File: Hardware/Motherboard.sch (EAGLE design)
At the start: 66 parts, among them J1 MICROMOD-2222-C, J10 MICRO-SD-PUSH-PUSH-EXT-PIN, J2 Vertical Qwiic Connector, J4 QWIIC_RIGHT_ANGLE, J5 CORTEX_JTAG_DEBUG_MINIMUM_PTH, J6 MICROMOD_CARRIER, J7 MICROMOD_CARRIER, U2 MCP73831, U5 AP7361C-33

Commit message: Adds second standoff for qwiic boards, attaches VIN net to processor connector
Deletes second page in schematic
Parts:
- removed FRAME2: FRAME-LEDGERNO_FOOTPRINT, SparkFun-Aesthetics:FRAME-LEDGERNO_FOOTPRINT
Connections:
- removed net USB_VIN: J1.USB_VIN
- net VIN: now also J1.USB_VIN
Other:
- note added: "Buttons"

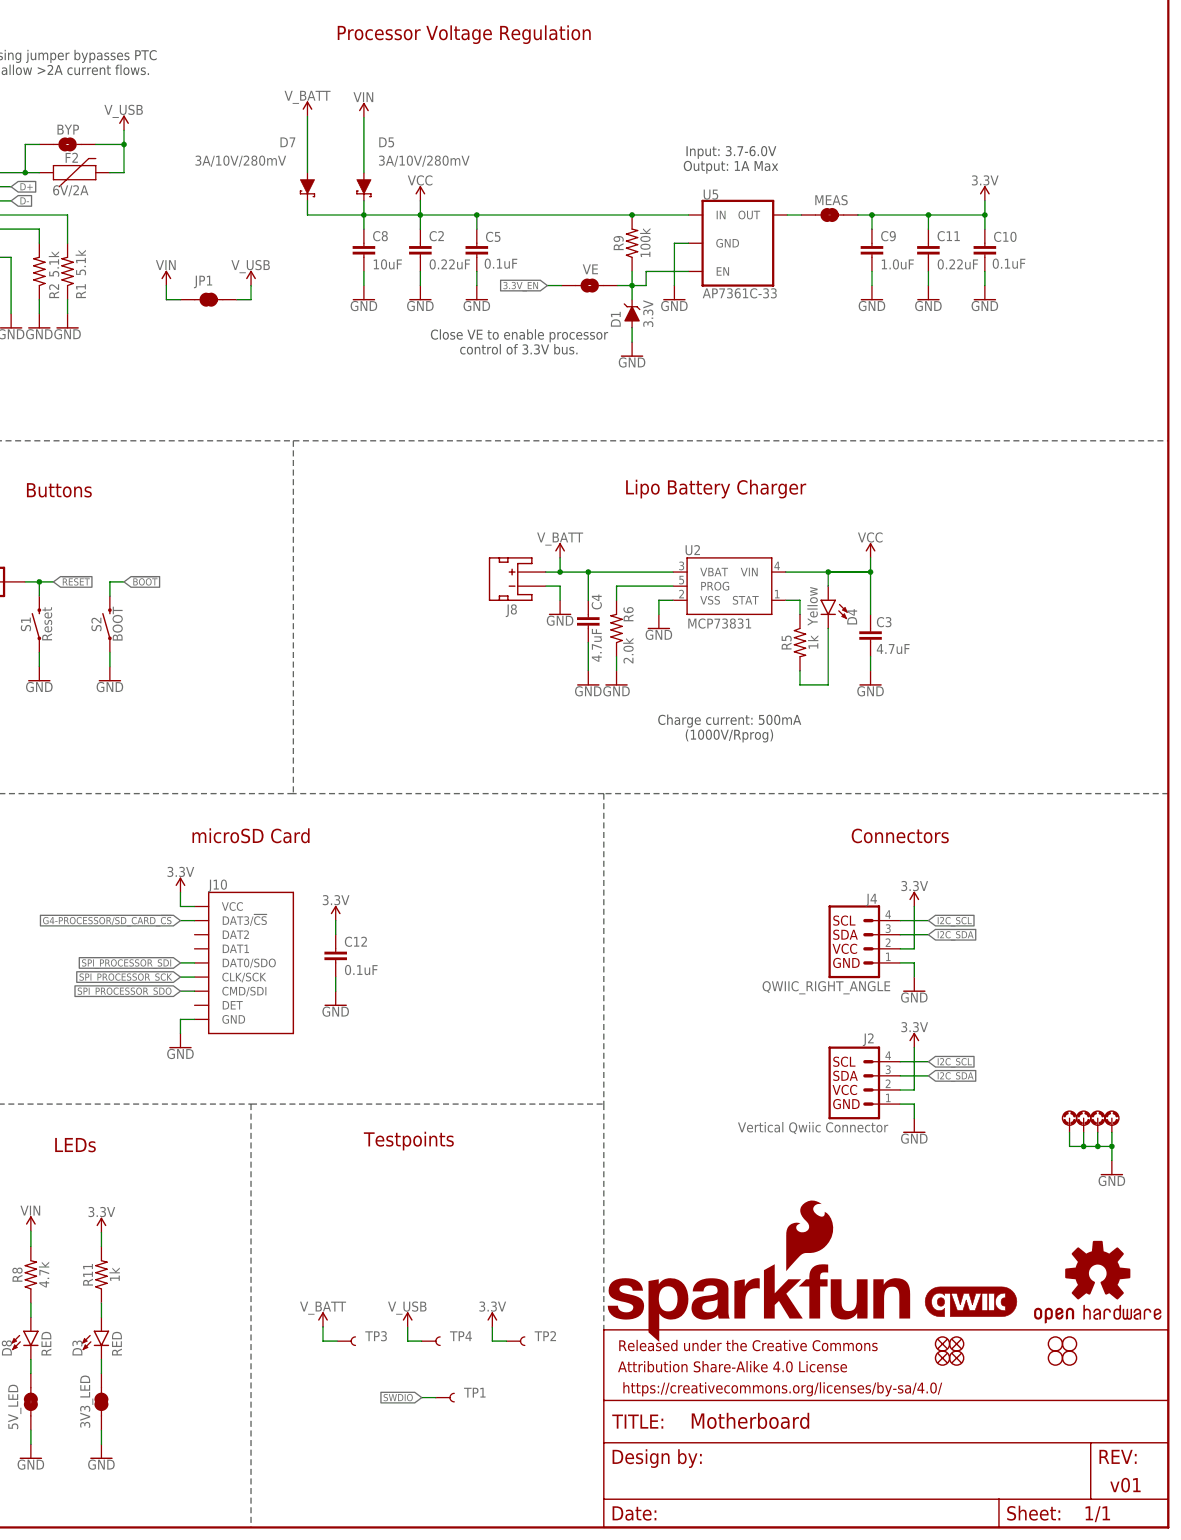
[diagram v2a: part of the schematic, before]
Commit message: Adds silk, removes "VIN/VUSB" jumper
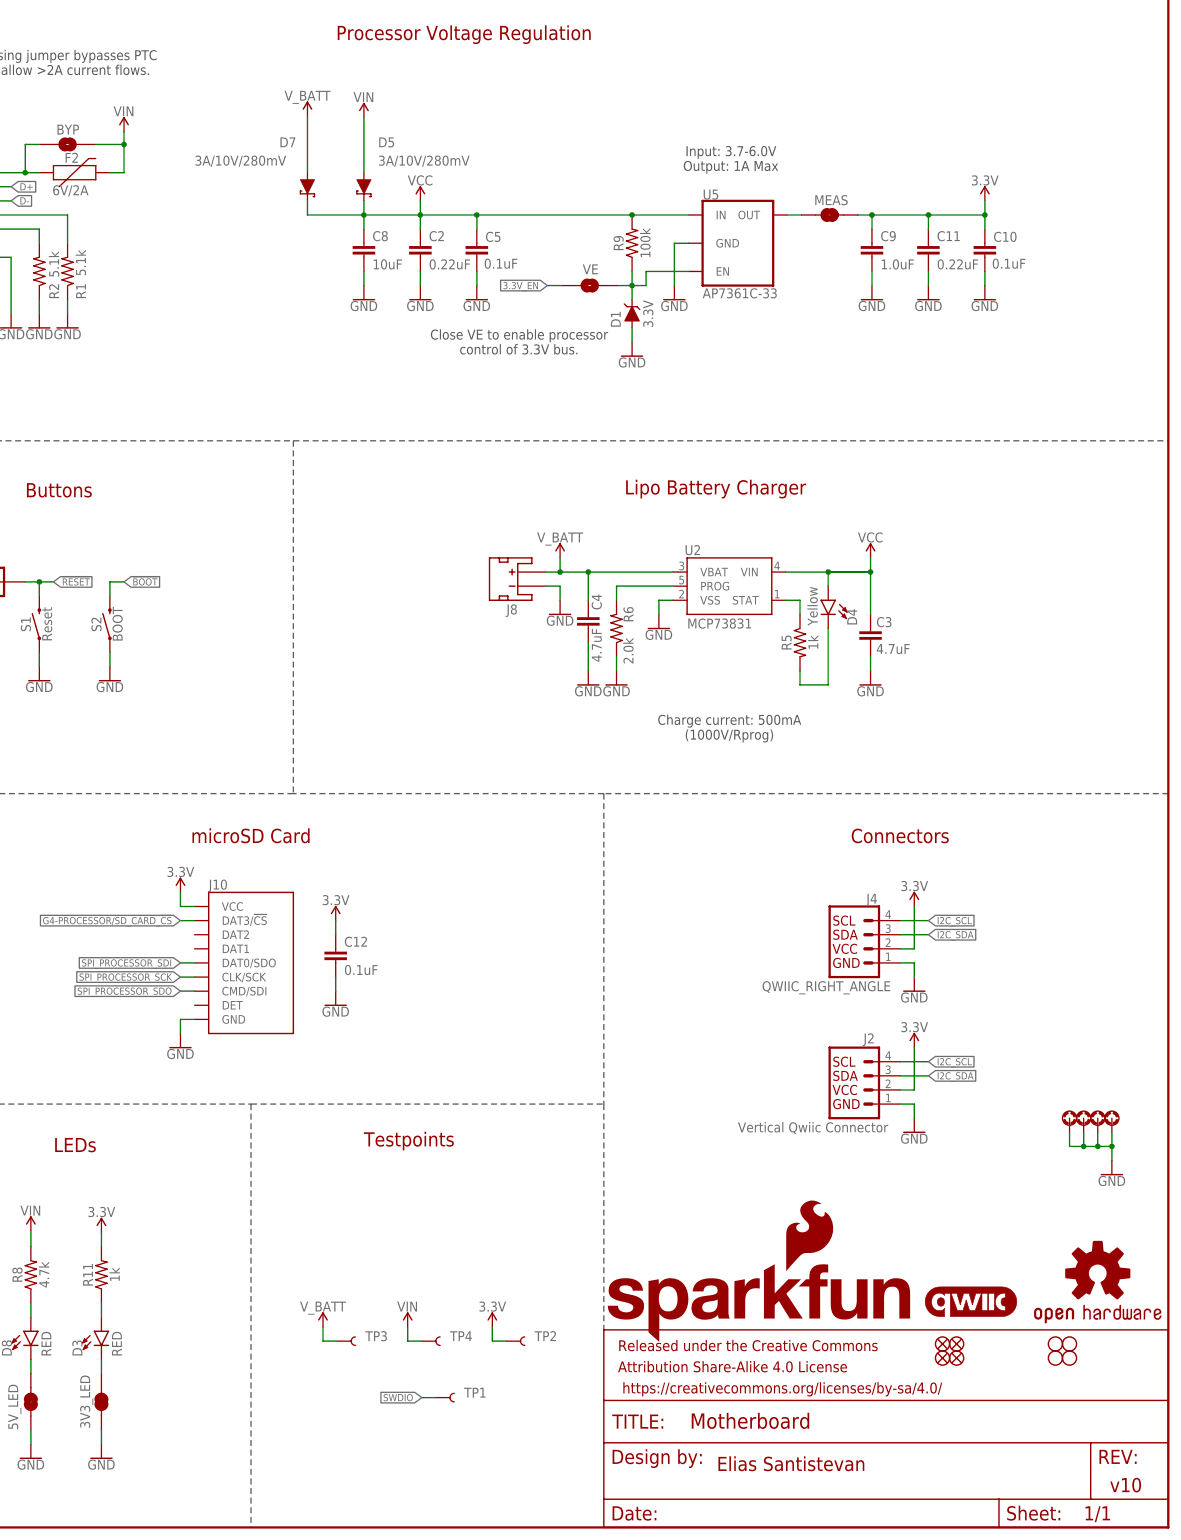
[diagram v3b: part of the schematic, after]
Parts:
- removed JP1: JUMPER-SMT_2_NC_TRACE_SILK, SparkFun-Jumpers:JUMPER-SMT_2_NC_TRACE_SILK
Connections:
- removed net V_USB: BYP.2, F2.2, JP1.2, TP4.1
- net VIN: now also BYP.2, F2.2, TP4.1; no longer JP1.1
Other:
- note added: "Elias Santistevan"
- note added: "v10"
- note removed: "v01"
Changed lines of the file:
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@@
 <?xml version="1.0" encoding="utf-8"?>
 <!DOCTYPE eagle SYSTEM "eagle.dtd">
-<eagle version="9.5.1">
+<eagle version="9.6.2">
 <drawing>
 <settings>
@@
 <part name="SUPPLY23" library="SparkFun-PowerSymbols" deviceset="VIN" device=""/>
 <part name="SUPPLY4" library="SparkFun-PowerSymbols" deviceset="VIN" device=""/>
-<part name="JP1" library="SparkFun-Jumpers" deviceset="JUMPER-SMT_2_NC_TRACE" device="_SILK" package3d_urn="urn:adsk.eagle:package:39281/1"/>
-<part name="SUPPLY18" library="SparkFun-PowerSymbols" deviceset="VIN" device=""/>
-<part name="SUPPLY21" library="SparkFun-PowerSymbols" deviceset="V_USB" device=""/>
 <part name="LOGO2" library="SparkFun-Aesthetics" deviceset="SFE_LOGO_NAME_FLAME" device=".3_INCH"/>
 <part name="LOGO3" library="SparkFun-Aesthetics" deviceset="OSHW-LOGO" device="S"/>
@@
 <part name="D8" library="SparkFun-LED" deviceset="LED-RED" device="0603" value="RED"/>
 <part name="GND39" library="SparkFun-PowerSymbols" deviceset="GND" device=""/>
-<part name="SUPPLY7" library="SparkFun-PowerSymbols" deviceset="V_USB" device=""/>
 <part name="SUPPLY13" library="SparkFun-PowerSymbols" deviceset="VIN" device=""/>
-<part name="SUPPLY8" library="SparkFun-PowerSymbols" deviceset="V_USB" device=""/>
 <part name="SUPPLY24" library="SparkFun-PowerSymbols" deviceset="VIN" device=""/>
+<part name="SUPPLY26" library="SparkFun-PowerSymbols" deviceset="VIN" device=""/>
+<part name="SUPPLY7" library="SparkFun-PowerSymbols" deviceset="VIN" device=""/>
 </parts>
 <sheets>
@@
 <text x="96.774" y="123.952" size="2.54" layer="94" font="vector" align="center">Function Board Connectors</text>
 <text x="95.25" y="271.526" size="2.54" layer="94" font="vector" align="center">Processor Board Connector</text>
-<text x="424.18" y="7.62" size="2.54" layer="94" font="vector" align="center">v01</text>
+<text x="424.18" y="7.62" size="2.54" layer="94" font="vector" align="center">v10</text>
 <wire x1="330.2" y1="132.08" x2="274.32" y2="132.08" width="0.2032" layer="97" style="longdash"/>
 <wire x1="274.32" y1="132.08" x2="205.74" y2="132.08" width="0.2032" layer="97" style="longdash"/>
@@
 <wire x1="274.32" y1="195.58" x2="274.32" y2="132.08" width="0.2032" layer="97" style="longdash"/>
 <text x="226.06" y="185.42" size="2.54" layer="94" font="vector">Buttons</text>
+<text x="350.52" y="10.16" size="2.54" layer="94" font="vector">Elias Santistevan</text>
 </plain>
 <instances>
@@
 <attribute name="VALUE" x="22.352" y="179.324" size="1.778" layer="96" align="bottom-center"/>
 </instance>
-<instance part="JP1" gate="G$1" x="259.08" y="220.98" smashed="yes">
-<attribute name="NAME" x="256.54" y="223.52" size="1.778" layer="95" font="vector"/>
-</instance>
-<instance part="SUPPLY18" gate="G$1" x="251.46" y="223.52" smashed="yes">
-<attribute name="VALUE" x="251.46" y="226.314" size="1.778" layer="96" align="bottom-center"/>
-</instance>
-<instance part="SUPPLY21" gate="G$1" x="266.7" y="223.52" smashed="yes">
-<attribute name="VALUE" x="266.7" y="226.314" size="1.778" layer="96" align="bottom-center"/>
-</instance>
 <instance part="LOGO2" gate="G$1" x="330.2" y="33.02" smashed="yes"/>
 <instance part="LOGO3" gate="G$1" x="419.1" y="45.72" smashed="yes"/>
@@
 <attribute name="VALUE" x="227.076" y="12.192" size="1.778" layer="96" font="vector" align="top-center"/>
 </instance>
-<instance part="SUPPLY7" gate="G$1" x="243.84" y="251.46" smashed="yes">
-<attribute name="VALUE" x="243.84" y="254.254" size="1.778" layer="96" align="bottom-center"/>
-</instance>
 <instance part="SUPPLY13" gate="G$1" x="287.02" y="253.746" smashed="yes">
 <attribute name="VALUE" x="287.02" y="256.54" size="1.778" layer="96" align="bottom-center"/>
 </instance>
-<instance part="SUPPLY8" gate="G$1" x="294.894" y="36.068" smashed="yes">
-<attribute name="VALUE" x="294.894" y="38.862" size="1.778" layer="96" align="bottom-center"/>
-</instance>
 <instance part="SUPPLY24" gate="G$1" x="227.076" y="53.34" smashed="yes">
 <attribute name="VALUE" x="227.076" y="56.134" size="1.778" layer="96" align="bottom-center"/>
+</instance>
+<instance part="SUPPLY26" gate="G$1" x="243.84" y="251.206" smashed="yes">
+<attribute name="VALUE" x="243.84" y="254" size="1.778" layer="96" align="bottom-center"/>
+</instance>
+<instance part="SUPPLY7" gate="G$1" x="294.894" y="36.068" smashed="yes">
+<attribute name="VALUE" x="294.894" y="38.862" size="1.778" layer="96" align="bottom-center"/>
 </instance>
 </instances>
@@
 </segment>
 <segment>
-<pinref part="JP1" gate="G$1" pin="1"/>
-<wire x1="254" y1="220.98" x2="251.46" y2="220.98" width="0.1524" layer="91"/>
-<wire x1="251.46" y1="220.98" x2="251.46" y2="223.52" width="0.1524" layer="91"/>
-<pinref part="SUPPLY18" gate="G$1" pin="VIN"/>
-</segment>
-<segment>
 <pinref part="J1" gate="J1" pin="USB_VIN"/>
 <wire x1="63.5" y1="231.14" x2="45.72" y2="231.14" width="0.1524" layer="91"/>
@@
 <pinref part="SUPPLY13" gate="G$1" pin="VIN"/>
 <wire x1="287.02" y1="243.84" x2="287.02" y2="253.746" width="0.1524" layer="91"/>
-</segment>
-</net>
-<net name="V_USB" class="0">
-<segment>
-<pinref part="JP1" gate="G$1" pin="2"/>
-<wire x1="264.16" y1="220.98" x2="266.7" y2="220.98" width="0.1524" layer="91"/>
-<wire x1="266.7" y1="220.98" x2="266.7" y2="223.52" width="0.1524" layer="91"/>
-<pinref part="SUPPLY21" gate="G$1" pin="V_USB"/>
 </segment>
 <segment>
@@
 <pinref part="F2" gate="F1" pin="2"/>
 <wire x1="243.84" y1="243.84" x2="241.3" y2="243.84" width="0.1524" layer="91"/>
-<pinref part="SUPPLY7" gate="G$1" pin="V_USB"/>
-<wire x1="243.84" y1="248.92" x2="243.84" y2="251.46" width="0.1524" layer="91"/>
+<pinref part="SUPPLY26" gate="G$1" pin="VIN"/>
+<wire x1="243.84" y1="248.92" x2="243.84" y2="251.206" width="0.1524" layer="91"/>
 <junction x="243.84" y="248.92"/>
 </segment>
@@
 <wire x1="297.434" y1="33.528" x2="294.894" y2="33.528" width="0.1524" layer="91"/>
 <wire x1="294.894" y1="33.528" x2="294.894" y2="36.068" width="0.1524" layer="91"/>
-<pinref part="SUPPLY8" gate="G$1" pin="V_USB"/>
-</segment>
-</net>
+<pinref part="SUPPLY7" gate="G$1" pin="VIN"/>
+</segment>
+</net>

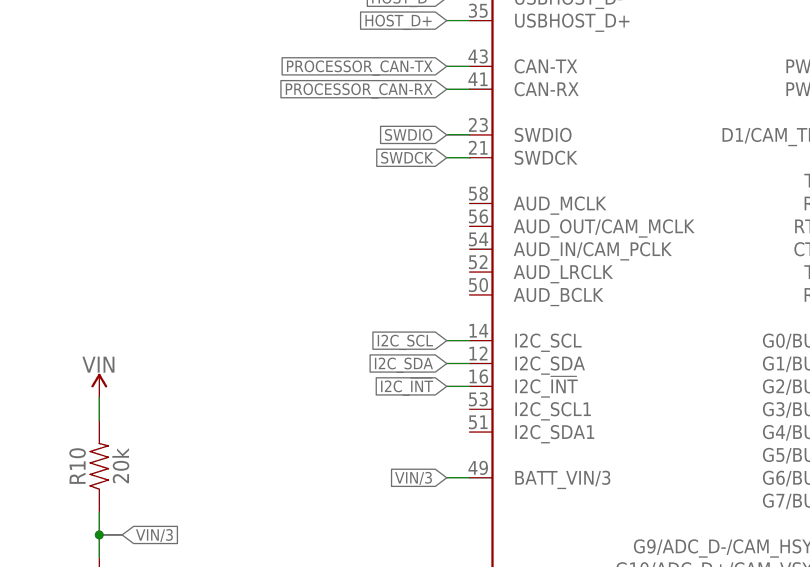
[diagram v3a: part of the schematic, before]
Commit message: Double routes power enable for ESP32 processor boards
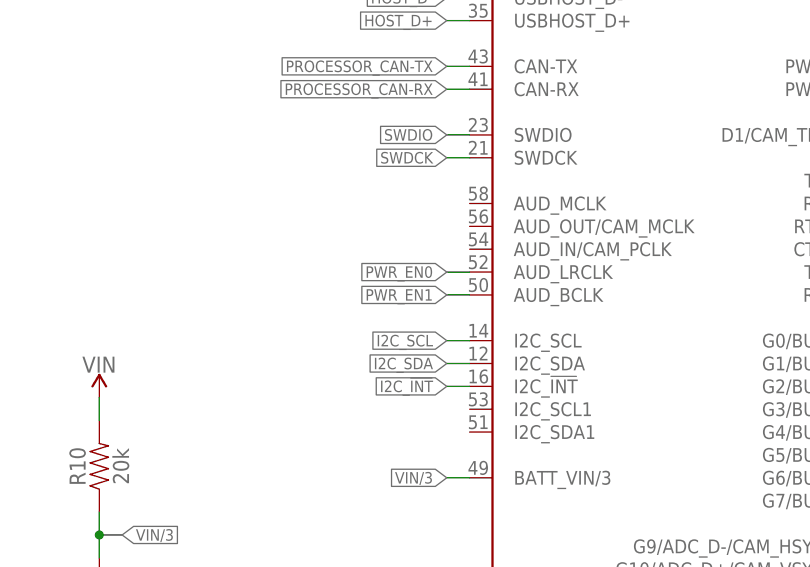
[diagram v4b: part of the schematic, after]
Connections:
- net PWR_EN0: now also J1.AUD_LRCLK
- net PWR_EN1: now also J1.AUD_BCLK
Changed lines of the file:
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@@
 <label x="111.76" y="238.76" size="1.27" layer="95" font="vector" xref="yes"/>
+</segment>
+<segment>
+<wire x1="63.5" y1="190.5" x2="60.96" y2="190.5" width="0.1524" layer="91"/>
+<label x="60.96" y="190.5" size="1.27" layer="95" font="vector" rot="R180" xref="yes"/>
+<pinref part="J1" gate="J1" pin="AUD_LRCLK"/>
 </segment>
 </net>
@@
 <label x="111.76" y="241.3" size="1.27" layer="95" font="vector" xref="yes"/>
 </segment>
+<segment>
+<wire x1="63.5" y1="187.96" x2="60.96" y2="187.96" width="0.1524" layer="91"/>
+<label x="60.96" y="187.96" size="1.27" layer="95" font="vector" rot="R180" xref="yes"/>
+<pinref part="J1" gate="J1" pin="AUD_BCLK"/>
+</segment>
 </net>
